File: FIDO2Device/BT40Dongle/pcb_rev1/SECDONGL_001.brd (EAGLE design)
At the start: 20 x 30 mm, 37 parts, among them CN1 CX60-24S-UNIT, CN2 IF_5PIN_H, CN3 IF_2PIN_SOL, SW1 SKRPACE010, SW3 SKTADAE010, U1 BT40, U2 ADP122ACPZ-3.3-R7, U3 RV-3028-C7

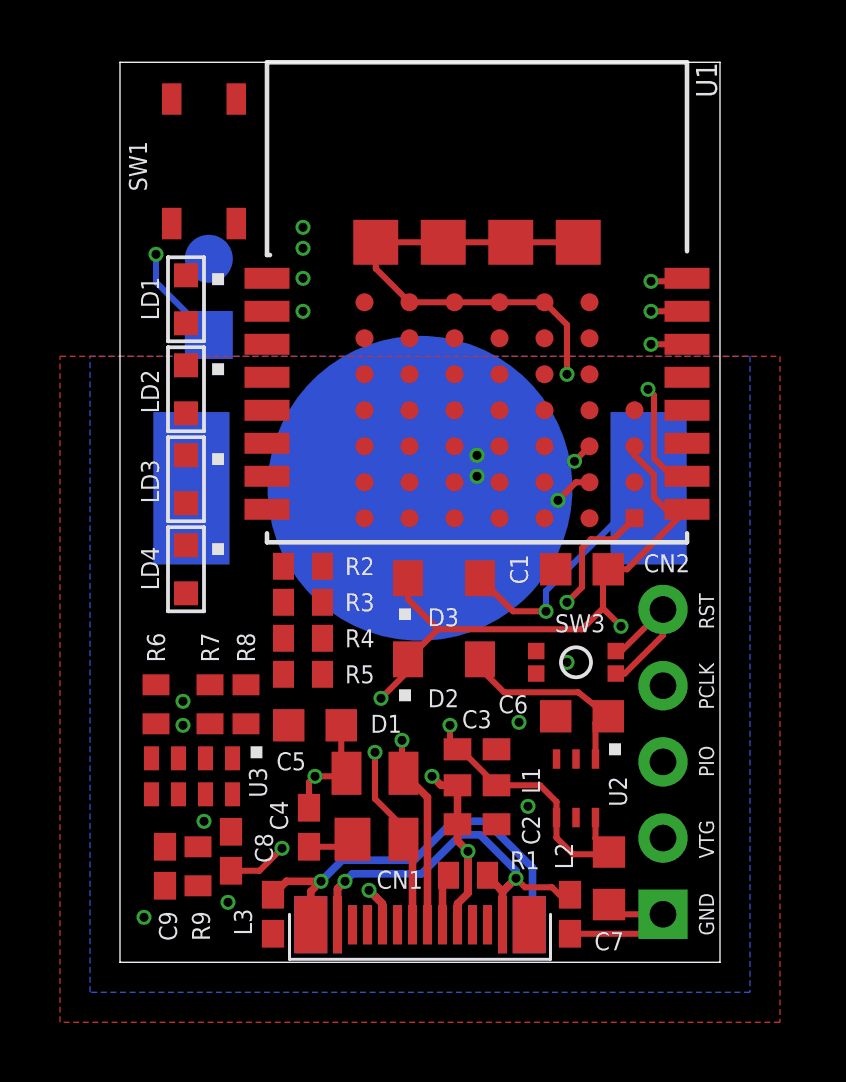
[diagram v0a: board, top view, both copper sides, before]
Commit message: 配線レイアウトを作成
・残りの信号／電源を配線
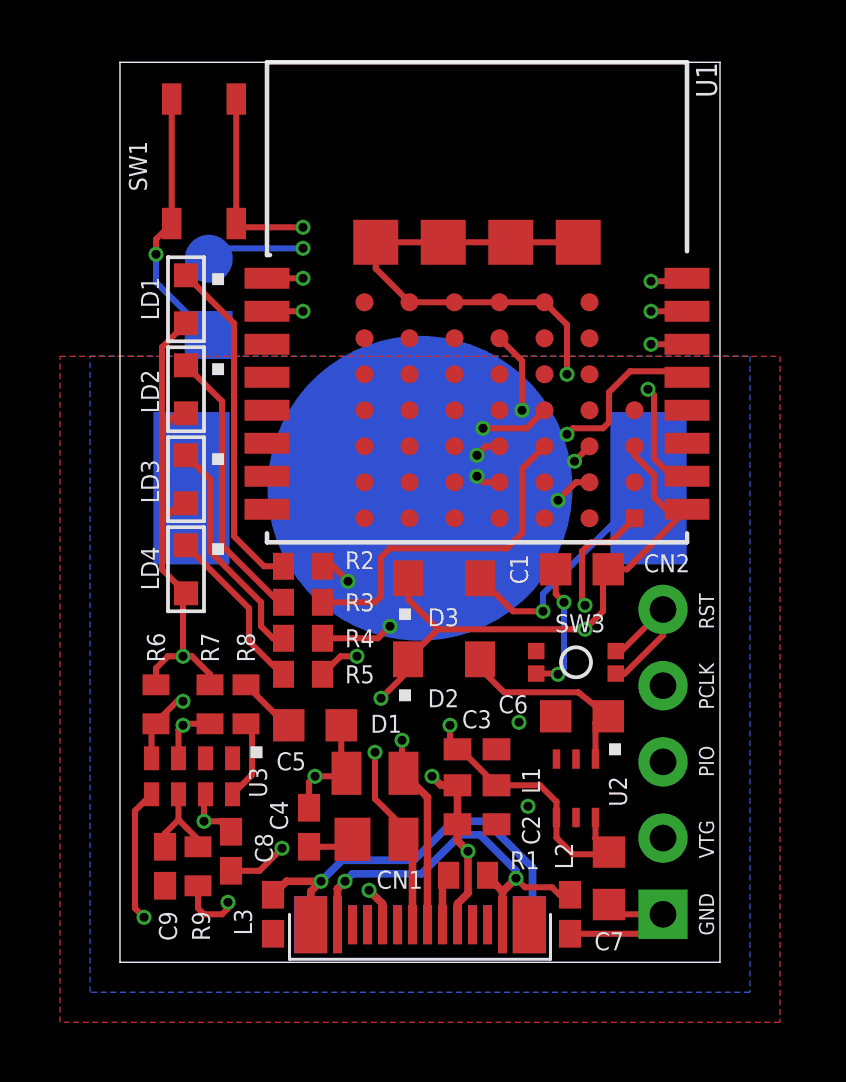
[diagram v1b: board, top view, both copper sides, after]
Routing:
- net VDD_NRF: track 35.1 -> 60.3 mm, vias 3 -> 4
- net SDA: track 0.00 -> 22.6 mm
- net SCL: track 0.00 -> 21.6 mm
- net SW1: track 0.00 -> 19.1 mm
- net LED3: track 0.00 -> 18.1 mm, vias 0 -> 2
- net 0V: track 32.4 -> 48.7 mm, vias 8 -> 9
- net LED4: track 0.00 -> 16.0 mm, vias 0 -> 2
- net TXD: track 0.00 -> 15.8 mm
- net LED1: track 0.00 -> 13.9 mm, vias 0 -> 2
- net LED2: track 0.00 -> 11.6 mm
- net N$8: track 0.00 -> 11.4 mm
- net N$7: track 0.00 -> 9.33 mm
- net N$6: track 0.00 -> 7.65 mm
- net N$1: track 0.00 -> 5.75 mm
- net N$4: track 0.00 -> 3.11 mm
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
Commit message: 配線レイアウトを作成
・レイアウトを横に0.4mm拡張
（べたGNDパターンが左右で途切れないようにするための措置）
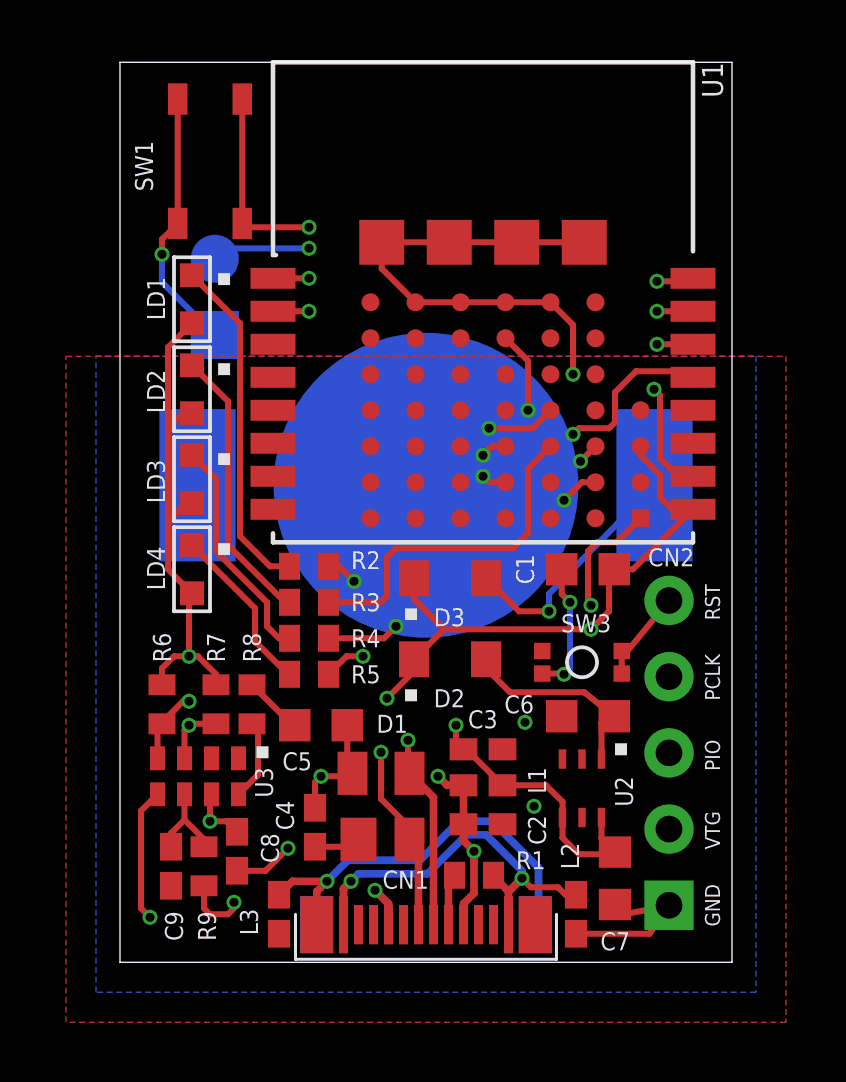
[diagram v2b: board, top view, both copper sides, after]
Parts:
- moved CN2 0.36 mm to (18.3, 1.90)
- moved BAT1 0.22 mm to (10.2, 15.9)
- moved R1 0.20 mm to (11.8, 2.90)
- moved SW3 0.20 mm to (15.4, 10.0)
- moved U2 0.20 mm to (15.4, 5.80)
- moved C4 0.20 mm to (6.50, 4.50)
- moved C5 0.20 mm to (6.70, 7.90)
- moved CN3 0.20 mm to (3.16, 20.9)
- moved L3 0.20 mm to (5.30, 1.60)
- moved R2 0.20 mm to (6.30, 13.2)
- moved R3 0.20 mm to (6.30, 12.0)
- moved R4 0.20 mm to (6.30, 10.8)
- moved R5 0.20 mm to (6.30, 9.60)
- moved R7 0.20 mm to (3.20, 8.60)
- moved R8 0.20 mm to (4.40, 8.60)
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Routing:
- net RESET: track 15.9 -> 13.7 mm
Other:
- board size 20 x 30 mm -> 20.4 x 30 mm

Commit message: 機能修正
・LEDの配線をいったん外す
（ブラインドviaが使用できないための措置）
・レイヤー設定を貫通viaのみの使用に戻す
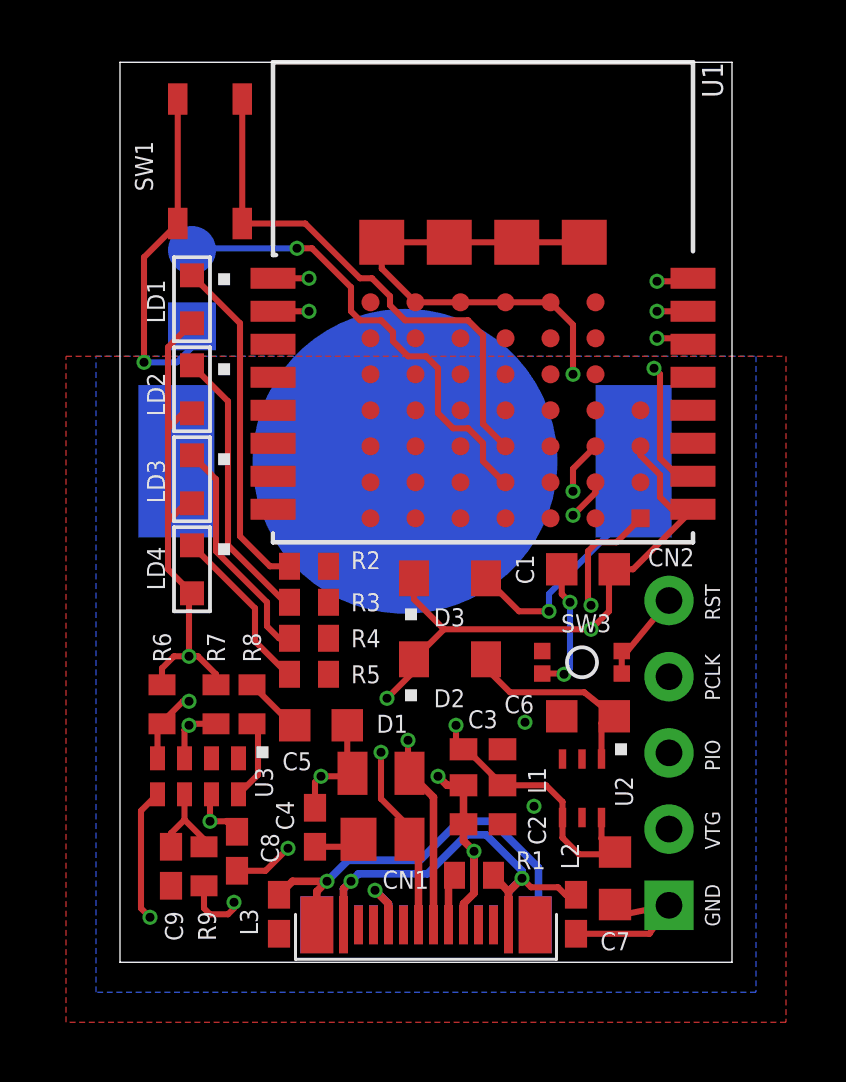
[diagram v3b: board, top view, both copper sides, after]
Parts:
- moved BAT1 1.06 mm to (9.50, 16.7)
- moved CN3 0.81 mm to (2.40, 21.2)
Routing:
- net LED3: track 18.1 -> 0.00 mm, vias 2 -> 0
- net LED4: track 16.0 -> 0.00 mm, vias 2 -> 0
- net LED1: track 13.9 -> 0.00 mm, vias 2 -> 0
- net LED2: track 11.6 -> 0.00 mm
- net 0V: track 49.0 -> 52.6 mm
- net SW1: track 19.1 -> 18.1 mm, vias 2 -> 0
- net VDD_BAT: track 26.0 -> 26.6 mm
- net TXD: track 15.8 -> 15.7 mm, vias 2 -> 1

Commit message: 配線レイアウトを修正
・LED1〜LED4を配線
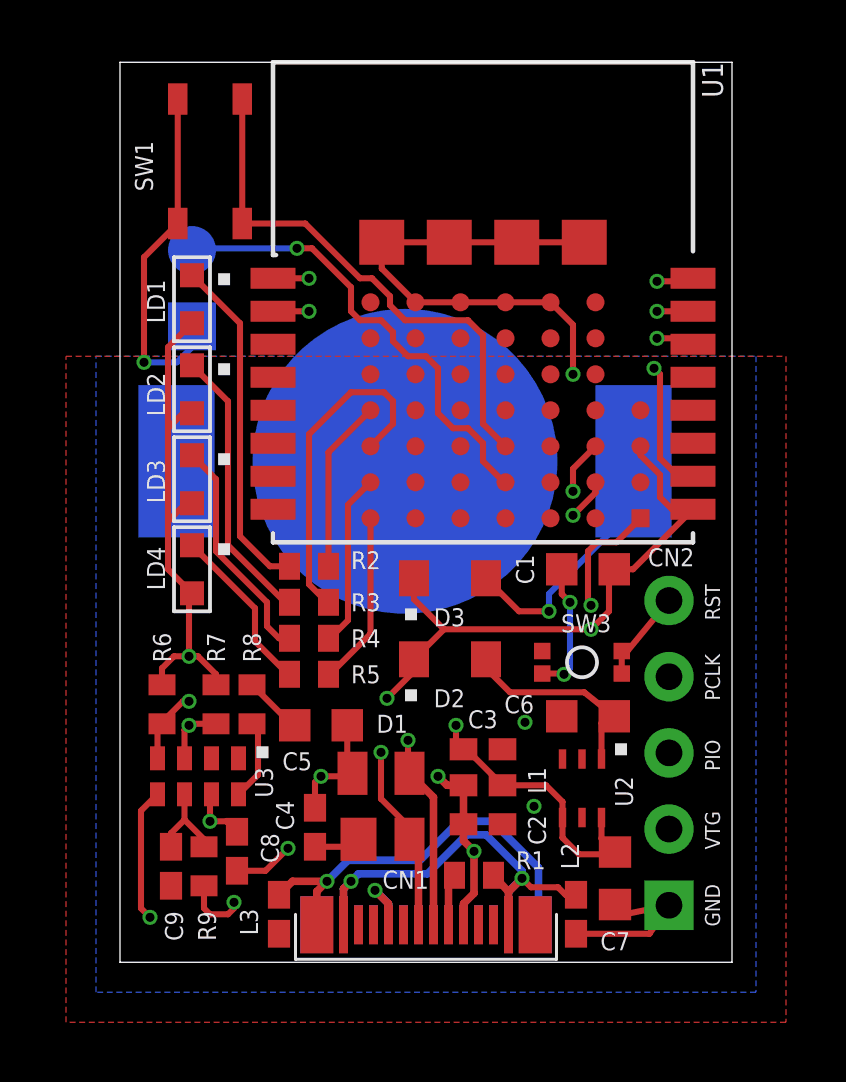
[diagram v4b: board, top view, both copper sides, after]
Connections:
- net LED1: now also U1.Z3; no longer U1.D3
- net LED2: now also U1.Z4; no longer U1.D4
- net LED3: now also U1.Z5; no longer U1.13
- net LED4: now also U1.Z6; no longer U1.C1
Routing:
- net LED2: track 0.00 -> 11.3 mm
- net LED3: track 0.00 -> 5.96 mm
- net LED4: track 0.00 -> 5.81 mm
- net LED1: track 0.00 -> 5.78 mm
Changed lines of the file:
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@@
 </signal>
 <signal name="LED4">
-<contactref element="U1" pad="C1"/>
 <contactref element="R5" pad="1"/>
-<wire x1="6.95" y1="9.6" x2="12.85" y2="20.8" width="0" layer="19" extent="1-1"/>
+<contactref element="U1" pad="Z6"/>
+<wire x1="6.95" y1="9.6" x2="7" y2="9.6" width="0.2032" layer="1"/>
+<wire x1="7" y1="9.6" x2="8.35" y2="10.95" width="0.2032" layer="1"/>
+<wire x1="8.35" y1="14.8" x2="8.35" y2="10.95" width="0.2032" layer="1"/>
 </signal>
 <signal name="LED3">
-<contactref element="U1" pad="13"/>
 <contactref element="R4" pad="1"/>
-<wire x1="6.95" y1="10.8" x2="19.1" y2="19.5" width="0" layer="19" extent="1-1"/>
+<contactref element="U1" pad="Z5"/>
+<wire x1="8.35" y1="16" x2="8.35" y2="16.15" width="0.2032" layer="1"/>
+<wire x1="6.95" y1="10.8" x2="7" y2="10.8" width="0.2032" layer="1"/>
+<wire x1="7" y1="10.8" x2="7.6" y2="11.4" width="0.2032" layer="1"/>
+<wire x1="7.6" y1="11.4" x2="7.6" y2="15.25" width="0.2032" layer="1"/>
+<wire x1="7.6" y1="15.25" x2="8.35" y2="16" width="0.2032" layer="1"/>
 </signal>
 <signal name="LED1">
-<contactref element="U1" pad="D3"/>
 <contactref element="R2" pad="1"/>
-<wire x1="6.95" y1="13.2" x2="14.35" y2="18.4" width="0" layer="19" extent="1-1"/>
+<contactref element="U1" pad="Z3"/>
+<wire x1="6.95" y1="13.2" x2="6.95" y2="17" width="0.2032" layer="1"/>
+<wire x1="6.95" y1="17" x2="8.35" y2="18.4" width="0.2032" layer="1"/>
 </signal>
 <signal name="LED2">
-<contactref element="U1" pad="D4"/>
 <contactref element="R3" pad="1"/>
-<wire x1="6.95" y1="12" x2="14.35" y2="17.2" width="0" layer="19" extent="1-1"/>
+<contactref element="U1" pad="Z4"/>
+<wire x1="6.95" y1="12" x2="7" y2="12" width="0.2032" layer="1"/>
+<wire x1="6.95" y1="12" x2="6.9" y2="12" width="0.2032" layer="1"/>
+<wire x1="6.9" y1="12" x2="6.3" y2="12.6" width="0.2032" layer="1"/>
+<wire x1="6.3" y1="12.6" x2="6.3" y2="17.6" width="0.2032" layer="1"/>
+<wire x1="6.3" y1="17.6" x2="7.7" y2="19" width="0.2032" layer="1"/>
+<wire x1="7.7" y1="19" x2="8.8" y2="19" width="0.2032" layer="1"/>
+<wire x1="8.8" y1="19" x2="9.1" y2="18.7" width="0.2032" layer="1"/>
+<wire x1="9.1" y1="18.7" x2="9.1" y2="17.95" width="0.2032" layer="1"/>
+<wire x1="9.1" y1="17.95" x2="8.35" y2="17.2" width="0.2032" layer="1"/>
 </signal>
 <signal name="TXD">

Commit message: 配線レイアウトを修正
・SW2のシルクがviaに重なっていた不具合を解消
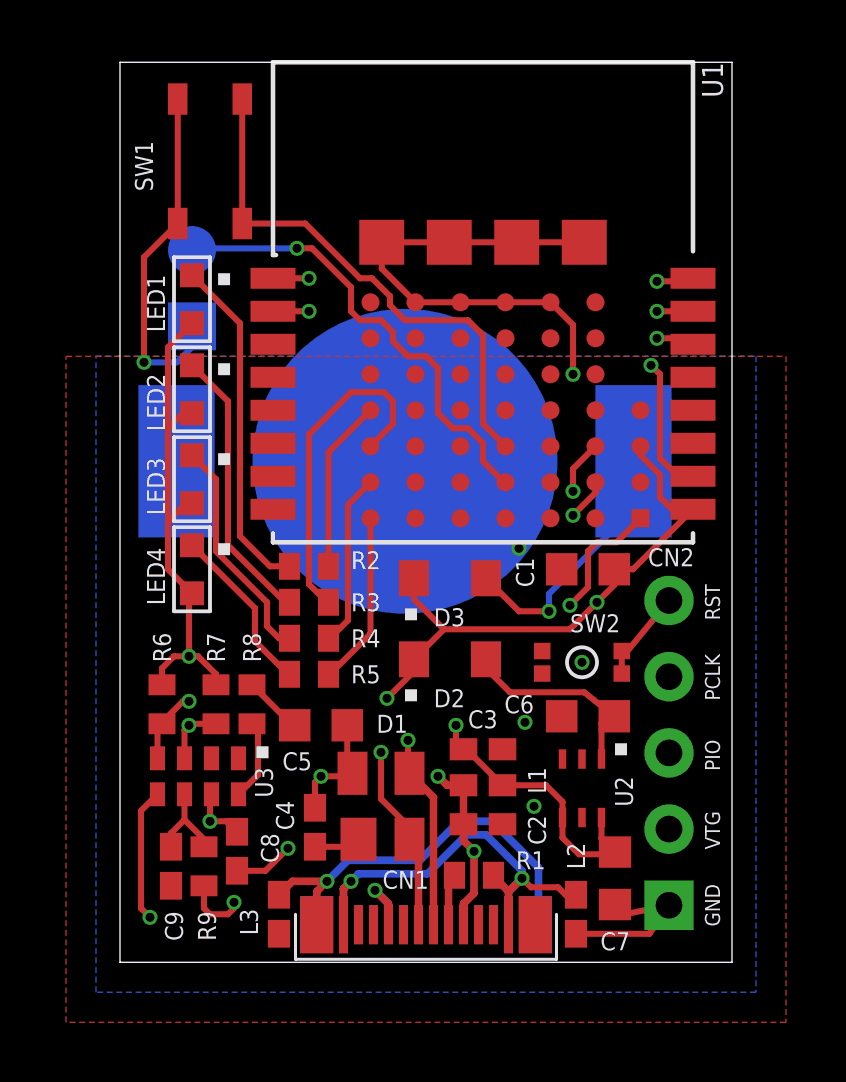
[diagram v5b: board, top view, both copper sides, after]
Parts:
- renumbered LD1 to LED1, LD2 to LED2, LD3 to LED3, LD4 to LED4, SW3 to SW2
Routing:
- net 0V: track 52.6 -> 48.3 mm
- net SWDIO: track 18.4 -> 19.3 mm
- net RESET: track 14.0 -> 13.3 mm

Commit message: 配線レイアウトを修正
・LED1 〜LED4が左側から順番に並ぶように修正
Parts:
- moved LED1 9.00 mm to (2.40, 13.1)
- moved LED4 9.00 mm to (2.40, 22.1)
- moved R2 3.60 mm to (6.30, 9.60)
- moved R5 3.60 mm to (6.30, 13.2)
- moved LED2 3.00 mm to (2.40, 16.1)
- moved LED3 3.00 mm to (2.40, 19.1)
- moved R3 1.20 mm to (6.30, 10.8)
- moved R4 1.20 mm to (6.30, 12.0)
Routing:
- net N$8: track 11.4 -> 5.68 mm
- net N$1: track 5.75 -> 11.5 mm
- net LED1: track 5.78 -> 9.92 mm
- net LED4: track 5.81 -> 2.74 mm
- net N$7: track 9.33 -> 7.45 mm
- net N$6: track 7.65 -> 9.33 mm
- net LED2: track 11.3 -> 10.0 mm
- net VDD_NRF: track 60.4 -> 61.4 mm

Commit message: 配線レイアウトを修正
・GNDのviaを追加
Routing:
- net 0V: track 48.3 -> 47.9 mm, vias 9 -> 21
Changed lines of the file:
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@@
 </element>
 <element name="R6" library="Parts" package="R0402" value="10k" x="1.4" y="8.6" smashed="yes" rot="R90">
-<attribute name="NAME" x="1.7" y="10" size="0.6" layer="25" rot="R90"/>
+<attribute name="NAME" x="1.8" y="10" size="0.6" layer="25" rot="R90"/>
 <attribute name="VALUE" x="2.82875" y="8.044375" size="0.7112" layer="27" rot="R90"/>
 </element>
@@
 <vertex x="-0.8" y="-1"/>
 </polygon>
-<via x="1" y="1.5" extent="1-16" drill="0.3"/>
+<via x="0.7" y="0.8" extent="1-16" drill="0.3"/>
 <polygon width="0.4064" layer="2" isolate="0.4064">
 <vertex x="-1.3" y="20.2"/>
@@
 <wire x1="1.25" y1="5.6" x2="0.7" y2="5.05" width="0.2032" layer="1"/>
 <wire x1="0.7" y1="5.05" x2="0.7" y2="1.8" width="0.2032" layer="1"/>
-<wire x1="0.7" y1="1.8" x2="1" y2="1.5" width="0.2032" layer="1"/>
 <wire x1="4.4" y1="9.25" x2="5.75" y2="7.9" width="0.2032" layer="1"/>
 <wire x1="5.75" y1="7.9" x2="5.825" y2="7.9" width="0.2032" layer="1"/>
@@
 <via x="15.4" y="10" extent="1-16" drill="0.3"/>
 <via x="13.3" y="13.8" extent="1-16" drill="0.3"/>
+<via x="0.7" y="4.8" extent="1-16" drill="0.3"/>
+<via x="0.7" y="2.8" extent="1-16" drill="0.3"/>
+<via x="3.6" y="0.8" extent="1-16" drill="0.3"/>
+<via x="0.8" y="10.4" extent="1-16" drill="0.3"/>
+<via x="14.5" y="3.3" extent="1-16" drill="0.3"/>
+<via x="19.7" y="0.8" extent="1-16" drill="0.3"/>
+<via x="19.7" y="3.1" extent="1-16" drill="0.3"/>
+<via x="19.7" y="5.7" extent="1-16" drill="0.3"/>
+<via x="19.7" y="8.2" extent="1-16" drill="0.3"/>
+<via x="19.7" y="10.8" extent="1-16" drill="0.3"/>
+<via x="19.7" y="13.3" extent="1-16" drill="0.3"/>
+<via x="13.9" y="6.9" extent="1-16" drill="0.3"/>
 </signal>
 <signal name="VBUS_NRF">

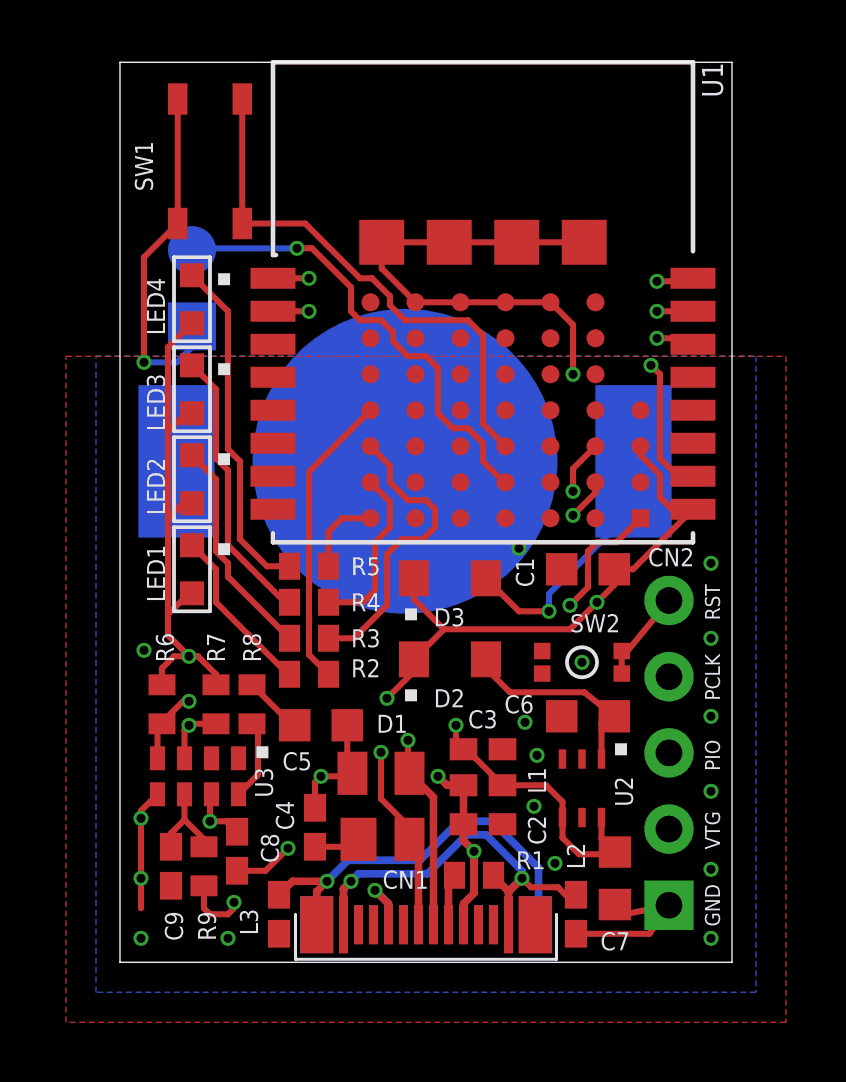
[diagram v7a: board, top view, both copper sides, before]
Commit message: 配線レイアウトを修正
・４層-->２層に変更
・これに伴い、デザインルール（DRC）を、２層用に差し替え
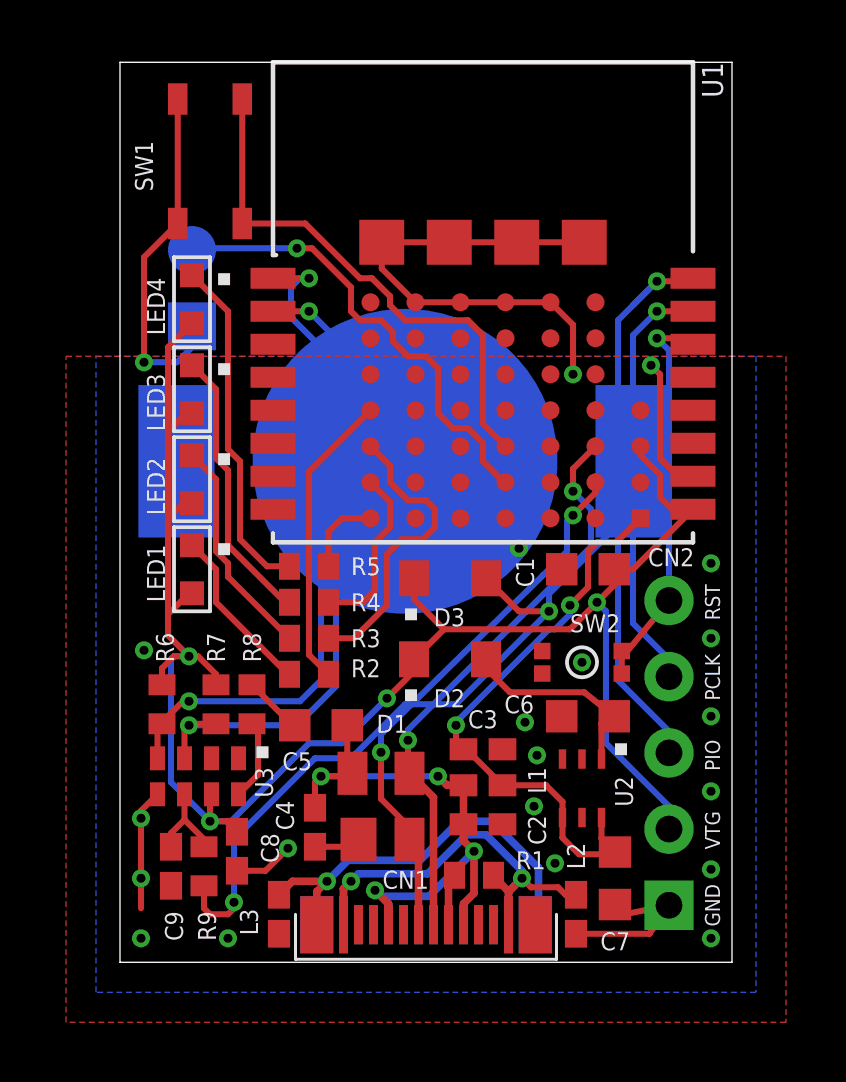
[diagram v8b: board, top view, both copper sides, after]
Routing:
- removed copper zone on layer 15, net 0V
- removed copper zone on layer 2, net 0V
